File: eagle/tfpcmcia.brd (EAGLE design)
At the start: 80.4 x 44.5 mm, 41 parts, among them IC1 CH32V467, IC2 LM1117MPX-3.3, J2 MSD-11-A

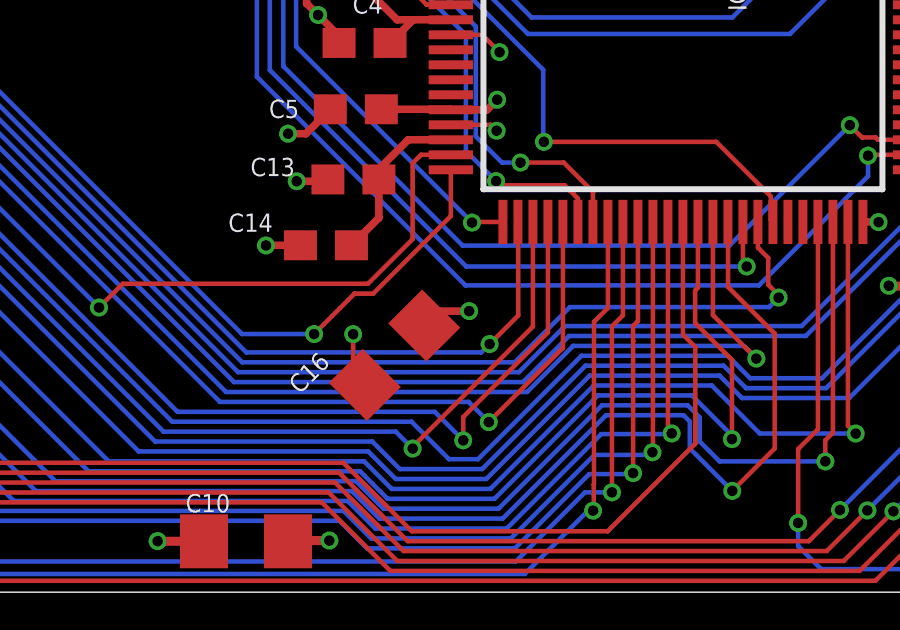
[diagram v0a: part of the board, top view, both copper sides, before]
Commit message: fixing the isolation width@ ~
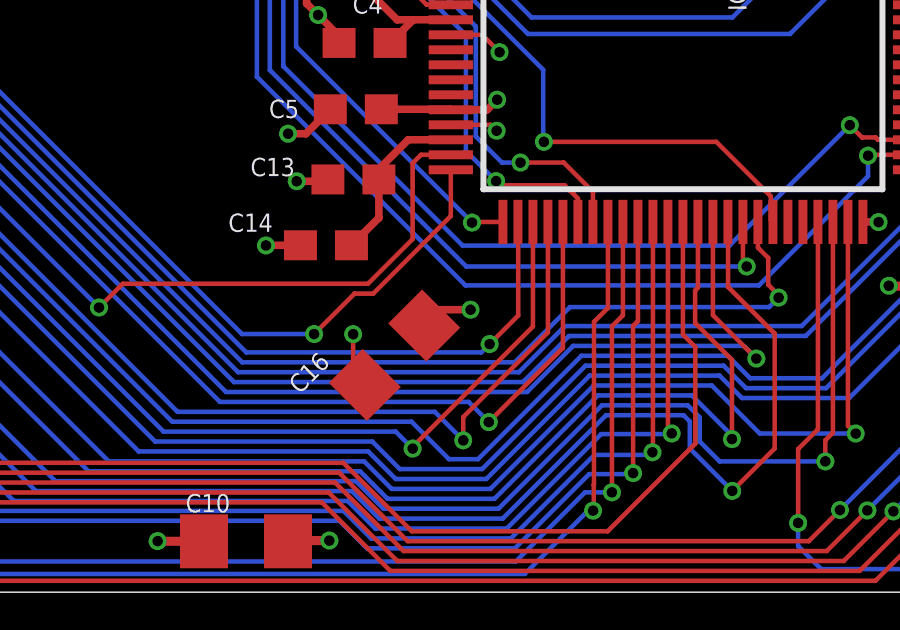
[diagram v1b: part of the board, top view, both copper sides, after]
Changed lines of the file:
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@@
 <contactref element="PCMCIA" pad="67"/>
 <contactref element="PCMCIA" pad="36"/>
-<polygon width="0" layer="15" isolate="0.4064">
+<polygon width="0.254" layer="15" isolate="0.4064">
 <vertex x="0" y="44.515021875"/>
 <vertex x="0" y="0"/>
@@
 <wire x1="28.841890625" y1="20.58000625" x2="29.59346875" y2="21.331584375" width="0.1524" layer="1"/>
 <via x="29.59346875" y="21.331584375" extent="1-16" drill="0.35"/>
+<wire x1="77.87264375" y1="40.001309375" x2="77.89335" y2="43.40259375" width="0" layer="19" extent="1-1"/>
+<wire x1="77.8704125" y1="36.57795" x2="77.87264375" y2="40.001309375" width="0" layer="19" extent="1-1"/>
+<wire x1="77.872775" y1="33.14148125" x2="77.8704125" y2="36.57795" width="0" layer="19" extent="1-1"/>
+<wire x1="77.048896875" y1="29.72518125" x2="77.049709375" y2="33.1142" width="0" layer="19" extent="1-1"/>
+<wire x1="77.0335" y1="26.296646875" x2="77.048896875" y2="29.72518125" width="0" layer="19" extent="1-1"/>
+<wire x1="77.921075" y1="22.82555" x2="77.905059375" y2="26.267825" width="0" layer="19" extent="1-1"/>
+<wire x1="77.93566875" y1="19.3627375" x2="77.921075" y2="22.82555" width="0" layer="19" extent="1-1"/>
+<wire x1="74.967265625" y1="16.087034375" x2="77.08543125" y2="19.359915625" width="0" layer="19" extent="1-1"/>
+<wire x1="72.326246875" y1="29.918096875" x2="77.048896875" y2="29.72518125" width="0" layer="19" extent="1-1"/>
+<wire x1="72.0607" y1="27.433190625" x2="72.326246875" y2="29.918096875" width="0" layer="19" extent="1-1"/>
+<wire x1="64.29554375" y1="24.1036875" x2="70.65648125" y2="27.37526875" width="0" layer="19" extent="1-1"/>
+<wire x1="67.872815625" y1="37.19351875" x2="70.542421875" y2="29.930871875" width="0" layer="19" extent="1-1"/>
+<wire x1="57.1720875" y1="37.517065625" x2="66.327596875" y2="37.18920625" width="0" layer="19" extent="1-1"/>
+<wire x1="46.0039375" y1="37.814890625" x2="56.0128125" y2="37.534696875" width="0" layer="19" extent="1-1"/>
+<wire x1="42.642890625" y1="30.565409375" x2="45.994621875" y2="36.794346875" width="0" layer="19" extent="1-1"/>
+<wire x1="42.743509375" y1="25.58000625" x2="43.400240625" y2="29.70823125" width="0" layer="19" extent="1-1"/>
+<wire x1="38.3987125" y1="31.296175" x2="42.642890625" y2="30.565409375" width="0" layer="19" extent="1-1"/>
+<wire x1="36.505509375" y1="27.81800625" x2="38.3987125" y2="31.296175" width="0" layer="19" extent="1-1"/>
+<wire x1="32.005509375" y1="27.81800625" x2="36.505509375" y2="27.81800625" width="0" layer="19" extent="1-1"/>
+<wire x1="28.7523125" y1="30.620171875" x2="31.722403125" y2="29.09045625" width="0" layer="19" extent="1-1"/>
+<wire x1="25.16115625" y1="28.7546375" x2="28.7523125" y2="30.620171875" width="0" layer="19" extent="1-1"/>
+<wire x1="25.849675" y1="25.72458125" x2="24.44473125" y2="28.082671875" width="0" layer="19" extent="1-1"/>
+<wire x1="29.59346875" y1="21.331584375" x2="27.267509375" y2="25.58000625" width="0" layer="19" extent="1-1"/>
+<wire x1="27.267509375" y1="18.58000625" x2="27.267509375" y2="20.58000625" width="0" layer="19" extent="1-1"/>
+<wire x1="28.796071875" y1="15.381128125" x2="28.892921875" y2="18.00040625" width="0" layer="19" extent="1-1"/>
+<wire x1="23.543496875" y1="18.30696875" x2="27.267509375" y2="18.58000625" width="0" layer="19" extent="1-1"/>
+<wire x1="23.2535625" y1="16.096934375" x2="23.543496875" y2="18.30696875" width="0" layer="19" extent="1-1"/>
+<wire x1="22.13143125" y1="13.697796875" x2="21.8439125" y2="15.2823" width="0" layer="19" extent="1-1"/>
+<wire x1="22.25594375" y1="11.563084375" x2="22.13143125" y2="13.697796875" width="0" layer="19" extent="1-1"/>
+<wire x1="24.012071875" y1="8.6005875" x2="22.25594375" y2="11.563084375" width="0" layer="19" extent="1-1"/>
+<wire x1="23.21934375" y1="1.721015625" x2="24.40168125" y2="6.908559375" width="0" layer="19" extent="1-1"/>
+<wire x1="48.549784375" y1="22.454765625" x2="42.743509375" y2="25.58000625" width="0" layer="19" extent="1-1"/>
+<wire x1="67.217265625" y1="6.317034375" x2="74.83153125" y2="14.841003125" width="0" layer="19" extent="1-1"/>
+<wire x1="61.674121875" y1="4.508403125" x2="65.753959375" y2="6.31023125" width="0" layer="19" extent="1-1"/>
+<wire x1="74.83153125" y1="3.036521875" x2="67.217265625" y2="6.317034375" width="0" layer="19" extent="1-1"/>
+<wire x1="13.599446875" y1="32.338225" x2="24.44473125" y2="28.082671875" width="0" layer="19" extent="1-1"/>
+<wire x1="6.112665625" y1="42.2489375" x2="13.615446875" y2="33.591284375" width="0" layer="19" extent="1-1"/>
+<wire x1="1.991615625" y1="43.04208125" x2="1.991615625" y2="41.77208125" width="0" layer="19" extent="1-16"/>
+<wire x1="44.649840625" y1="10.20089375" x2="48.61005625" y2="21.304909375" width="0" layer="19" extent="1-1"/>
+<wire x1="48.624440625" y1="3.44485625" x2="44.491740625" y2="9.225209375" width="0" layer="19" extent="1-1"/>
+<wire x1="5.16691875" y1="1.8724625" x2="21.841275" y2="1.695921875" width="0" layer="19" extent="1-1"/>
+<wire x1="4.6208" y1="1.131875" x2="5.16691875" y2="1.8724625" width="0" layer="19" extent="1-1"/>
 </signal>
 <signal name="D3">
@@
 <wire x1="77.055525" y1="24.467825" x2="77.043346875" y2="24.480003125" width="0.1524" layer="1"/>
 <via x="77.043346875" y="24.480003125" extent="1-16" drill="0.35"/>
-<polygon width="0" layer="2" isolate="0.254" rank="2">
+<polygon width="0.254" layer="2" isolate="0.254" rank="2">
 <vertex x="0" y="44.515021875"/>
 <vertex x="0" y="0"/>
@@
 <wire x1="77.061875" y1="17.5627375" x2="77.0617875" y2="17.562825" width="0.1524" layer="1"/>
 <via x="77.0617875" y="17.562825" extent="1-16" drill="0.35"/>
+<wire x1="77.87264375" y1="38.201309375" x2="77.89335" y2="41.60259375" width="0" layer="19" extent="1-1"/>
+<wire x1="77.050309375" y1="34.799334375" x2="77.056446875" y2="38.1971125" width="0" layer="19" extent="1-1"/>
+<wire x1="77.872775" y1="31.34148125" x2="77.8704125" y2="34.77795" width="0" layer="19" extent="1-1"/>
+<wire x1="77.880025" y1="27.906359375" x2="77.872775" y2="31.34148125" width="0" layer="19" extent="1-1"/>
+<wire x1="77.043346875" y1="24.480003125" x2="77.063415625" y2="27.86235" width="0" layer="19" extent="1-1"/>
+<wire x1="77.921075" y1="21.02555" x2="77.905059375" y2="24.467825" width="0" layer="19" extent="1-1"/>
+<wire x1="77.93566875" y1="17.5627375" x2="77.921075" y2="21.02555" width="0" layer="19" extent="1-1"/>
+<wire x1="72.326246875" y1="34.540096875" x2="77.050309375" y2="34.799334375" width="0" layer="19" extent="1-1"/>
+<wire x1="72.05875" y1="37.181059375" x2="72.326246875" y2="34.540096875" width="0" layer="19" extent="1-1"/>
+<wire x1="46.0039375" y1="39.514890625" x2="70.672815625" y2="37.19351875" width="0" layer="19" extent="1-1"/>
+<wire x1="10.815446875" y1="33.591284375" x2="46.0039375" y2="39.514890625" width="0" layer="19" extent="1-1"/>
+<wire x1="4.3612875" y1="21.45518125" x2="9.29849375" y2="33.30924375" width="0" layer="19" extent="1-1"/>
+<wire x1="17.49550625" y1="1.70174375" x2="4.3612875" y2="21.45518125" width="0" layer="19" extent="1-1"/>
 </signal>
 <signal name="A16">
@@
 <via x="36.389234375" y="30.093128125" extent="1-16" drill="0.35"/>
 <wire x1="24.9535625" y1="16.096934375" x2="27.25058125" y2="16.096934375" width="0.254" layer="1"/>
-<wire x1="26.381578125" y1="8.88845625" x2="26.86289375" y2="9.369771875" width="0.254" layer="1"/>
-<wire x1="26.86289375" y1="9.369771875" x2="27.879315625" y2="9.369771875" width="0.254" layer="1"/>
-<via x="27.879315625" y="9.369771875" extent="1-16" drill="0.35"/>
+<wire x1="26.381578125" y1="8.88845625" x2="26.90883125" y2="9.415709375" width="0.254" layer="1"/>
+<wire x1="26.90883125" y1="9.415709375" x2="27.92525" y2="9.415709375" width="0.254" layer="1"/>
+<via x="27.92525" y="9.415709375" extent="1-16" drill="0.35"/>
 <wire x1="28.477103125" y1="16.08000625" x2="27.267509375" y2="16.08000625" width="0.254" layer="1"/>
 <wire x1="27.267509375" y1="16.08000625" x2="27.25058125" y2="16.096934375" width="0.254" layer="1"/>
